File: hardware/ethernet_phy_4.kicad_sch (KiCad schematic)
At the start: 31 parts, among them J3 RJMG1S8008101BR, SW2 SW TACT-SPST, U2 DP83826IRHBR, Y2 Crystal

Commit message: Design Schematic for STM32F407
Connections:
- net RX_D4 is gone; now on net RX_D3: U2.13 (RX_D3)
- net RX_D3: no longer U2.14 (RX_D2)
- new net RX_D2: U2.14 (RX_D2)
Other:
- moved on the sheet: D6, R8
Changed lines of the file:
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@@
 	)
 	(junction
+		(at 157.48 95.25)
+		(diameter 0)
+		(color 0 0 0 0)
+	)
+	(junction
 		(at 214.63 39.37)
 		(diameter 0)
@@
 	(wire
 		(pts
-			(xy 86.36 57.15) (xy 93.98 57.15)
+			(xy 88.9 57.15) (xy 93.98 57.15)
 		)
 		(stroke
@@
 	(wire
 		(pts
-			(xy 166.37 114.3) (xy 166.37 113.03)
+			(xy 165.1 114.3) (xy 165.1 113.03)
 		)
 		(stroke
@@
 	(wire
 		(pts
+			(xy 41.91 64.77) (xy 46.99 64.77)
+		)
+		(stroke
+			(width 0)
+			(type default)
+		)
+	)
+	(wire
+		(pts
 			(xy 151.13 80.01) (xy 149.86 80.01)
 		)
@@
 	(wire
 		(pts
-			(xy 166.37 96.52) (xy 166.37 92.71)
+			(xy 165.1 96.52) (xy 165.1 92.71)
 		)
 		(stroke
@@
 	(wire
 		(pts
-			(xy 166.37 105.41) (xy 166.37 104.14)
+			(xy 165.1 105.41) (xy 165.1 104.14)
 		)
 		(stroke
@@
 	(wire
 		(pts
-			(xy 45.72 64.77) (xy 46.99 64.77)
-		)
-		(stroke
-			(width 0)
-			(type default)
-		)
-	)
-	(wire
-		(pts
 			(xy 87.63 72.39) (xy 93.98 72.39)
 		)
@@
 	(wire
 		(pts
-			(xy 166.37 92.71) (xy 149.86 92.71)
+			(xy 165.1 92.71) (xy 149.86 92.71)
 		)
 		(stroke
@@
 	(wire
 		(pts
+			(xy 158.75 95.25) (xy 157.48 95.25)
+		)
+		(stroke
+			(width 0)
+			(type default)
+		)
+	)
+	(wire
+		(pts
 			(xy 214.63 46.99) (xy 214.63 53.34)
 		)
@@
 		)
 	)
-	(label "COL"
-		(at 157.48 92.71 180)
-		(effects
-			(font
-				(size 1.27 1.27)
-			)
-			(justify right bottom)
-		)
-	)
 	(label "RD_P"
 		(at 87.63 69.85 0)
@@
 		)
 	)
-	(label "CRS"
-		(at 157.48 95.25 180)
-		(effects
-			(font
-				(size 1.27 1.27)
-			)
-			(justify right bottom)
-		)
-	)
 	(label "TD_N"
 		(at 87.63 80.01 0)
@@
 		)
 	)
+	(label "INT"
+		(at 88.9 57.15 0)
+		(effects
+			(font
+				(size 1.27 1.27)
+			)
+			(justify left bottom)
+		)
+	)
 	(label "TD_N"
 		(at 88.9 158.75 180)
@@
 		)
 	)
+	(label "INT"
+		(at 41.91 64.77 0)
+		(effects
+			(font
+				(size 1.27 1.27)
+			)
+			(justify left bottom)
+		)
+	)
 	(label "DP83826IRHBR_OSC_OUT"
 		(at 125.73 118.11 180)
@@
 		)
 	)
-	(hierarchical_label "RX_D3"
+	(hierarchical_label "CRS"
+		(shape input)
+		(at 158.75 95.25 0)
+		(effects
+			(font
+				(size 1.27 1.27)
+			)
+			(justify left)
+		)
+	)
+	(hierarchical_label "RX_D2"
 		(shape input)
 		(at 151.13 62.23 0)
@@
 		)
 	)
-	(hierarchical_label "RX_D4"
+	(hierarchical_label "RX_D3"
 		(shape input)
 		(at 151.13 64.77 0)
@@
 		)
 	)
-	(hierarchical_label "RX_D0"
+	(hierarchical_label "COL"
 		(shape input)
-		(at 151.13 57.15 0)
+		(at 165.1 92.71 0)
 		(effects
 			(font
@@
 		)
 	)
-	(hierarchical_label "TX_D3"
+	(hierarchical_label "RX_D0"
 		(shape input)
-		(at 151.13 82.55 0)
+		(at 151.13 57.15 0)
 		(effects
 			(font
@@
 		)
 	)
-	(hierarchical_label "RX_CLK"
+	(hierarchical_label "TX_D3"
 		(shape input)
-		(at 151.13 49.53 0)
+		(at 151.13 82.55 0)
 		(effects
 			(font
@@
 		)
 	)
-	(hierarchical_label "INT"
+	(hierarchical_label "RX_CLK"
 		(shape input)
-		(at 45.72 64.77 180)
+		(at 151.13 49.53 0)
 		(effects
 			(font
 				(size 1.27 1.27)
 			)
-			(justify right)
+			(justify left)
 		)
 	)
@@
 		)
 	)
-	(hierarchical_label "INT"
-		(shape input)
-		(at 86.36 57.15 180)
-		(effects
-			(font
-				(size 1.27 1.27)
-			)
-			(justify right)
-		)
-	)
 	(symbol
 		(lib_id "power:VDD")
@@
 	(symbol
 		(lib_id "STM32F407 Dev Kit Library:LED")
-		(at 166.37 109.22 90)
+		(at 165.1 109.22 90)
 		(unit 1)
 		(body_style 1)
@@
 		(dnp no)
 		(property "Reference" "D6"
-			(at 167.894 108.204 90)
+			(at 166.624 108.204 90)
 			(show_name no)
 			(do_not_autoplace no)
@@
 		)
 		(property "Value" "RED"
-			(at 167.894 110.744 90)
+			(at 166.624 110.744 90)
 			(show_name no)
 			(do_not_autoplace no)
@@
 		)
 		(property "Footprint" ""
-			(at 166.37 109.22 0)
+			(at 165.1 109.22 0)
 			(hide yes)
 			(show_name no)
@@
 		)
 		(property "Datasheet" ""
-			(at 166.37 109.22 0)
+			(at 165.1 109.22 0)
 			(hide yes)
 			(show_name no)
@@
 		)
 		(property "Description" "Light emitting diode"
-			(at 166.37 109.22 0)
+			(at 165.1 109.22 0)
 			(hide yes)
 			(show_name no)
@@
 		)
 		(property "Sim.Pins" "1=K 2=A"
-			(at 166.37 109.22 0)
+			(at 165.1 109.22 0)
 			(hide yes)
 			(show_name no)
@@
 	(symbol
 		(lib_id "power:GND")
-		(at 166.37 114.3 0)
+		(at 165.1 114.3 0)
 		(unit 1)
 		(body_style 1)
@@
 		(fields_autoplaced yes)
 		(property "Reference" "#PWR020"
-			(at 166.37 120.65 0)
+			(at 165.1 120.65 0)
 			(hide yes)
 			(show_name no)
@@
 		)
 		(property "Value" "GND"
-			(at 166.37 119.38 0)
+			(at 165.1 119.38 0)
 			(show_name no)
 			(do_not_autoplace no)
@@
 		)
 		(property "Footprint" ""
-			(at 166.37 114.3 0)
+			(at 165.1 114.3 0)
 			(hide yes)
 			(show_name no)
@@
 		)
 		(property "Datasheet" ""
-			(at 166.37 114.3 0)
+			(at 165.1 114.3 0)
 			(hide yes)
 			(show_name no)
@@
 		)
 		(property "Description" "Power symbol creates a global label with name \"GND\" , ground"
-			(at 166.37 114.3 0)
+			(at 165.1 114.3 0)
 			(hide yes)
 			(show_name no)
@@
 	(symbol
 		(lib_id "STM32F407 Dev Kit Library:R")
-		(at 166.37 100.33 0)
+		(at 165.1 100.33 0)
 		(unit 1)
 		(body_style 1)
@@
 		(dnp no)
 		(property "Reference" "R8"
-			(at 168.656 99.06 0)
+			(at 167.386 99.06 0)
 			(show_name no)
 			(do_not_autoplace no)
@@
 		)
 		(property "Value" "3k3"
-			(at 168.656 101.6 0)
+			(at 167.386 101.6 0)
 			(show_name no)
 			(do_not_autoplace no)
@@
 		)
 		(property "Footprint" ""
-			(at 164.592 100.33 90)
+			(at 163.322 100.33 90)
 			(hide yes)
 			(show_name no)
@@
 		)
 		(property "Datasheet" ""
-			(at 166.37 100.33 0)
+			(at 165.1 100.33 0)
 			(hide yes)
 			(show_name no)
@@
 		)
 		(property "Description" "Resistor"
-			(at 166.37 100.33 0)
+			(at 165.1 100.33 0)
 			(hide yes)
 			(show_name no)

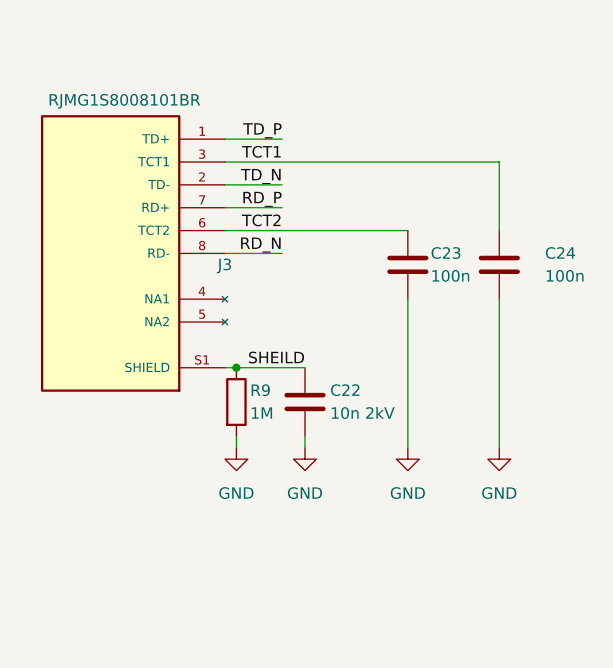
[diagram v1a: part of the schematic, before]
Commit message: Complete Schematic for Power Section
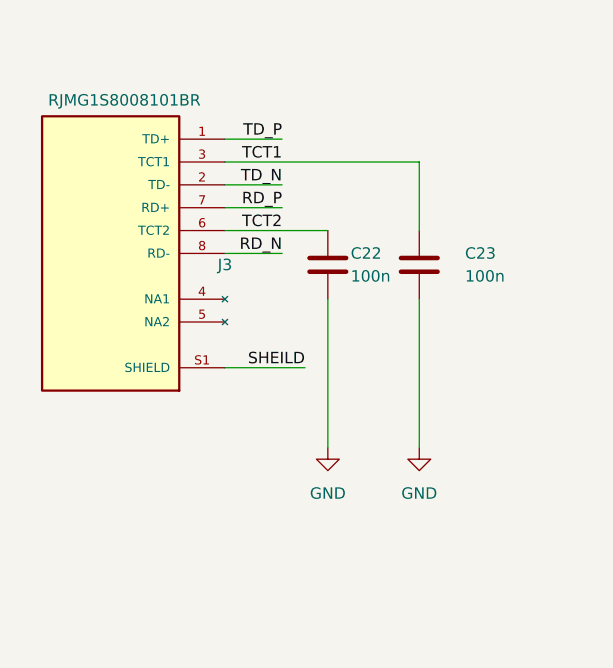
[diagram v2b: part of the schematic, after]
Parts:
- removed C22: 10n 2kV, Package_QFP:LQFP-48_7x7mm_P0.5mm, symbol STM32F407 Dev Kit Library:C
- removed R9: 1M, symbol STM32F407 Dev Kit Library:R
- renumbered C23 to C22, C24 to C23
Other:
- moved on the sheet: C22, C23

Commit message: Organize schematic
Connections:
- net GND: now also D1.2 (A), D2.2 (A), D3.2 (A), D4.2 (A)
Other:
- note added: "ESD"
- note added: "Ethernet PHY"
- note added: "Oscilator"
- note added: "RJ45 Jack"
- moved on the sheet: C11, C12, C13, C14, C15, C16, C17, C18, C19, C20, C21, C22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

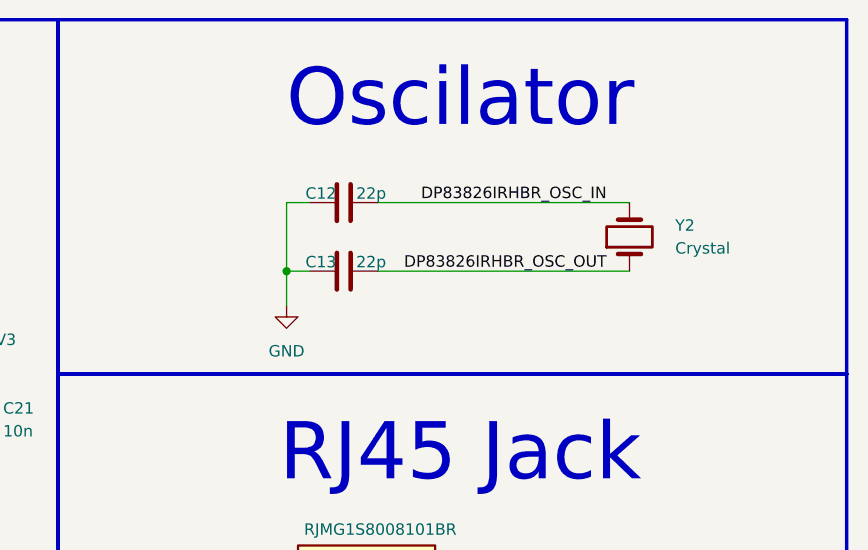
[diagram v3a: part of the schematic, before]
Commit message: Link footprints to Symbols
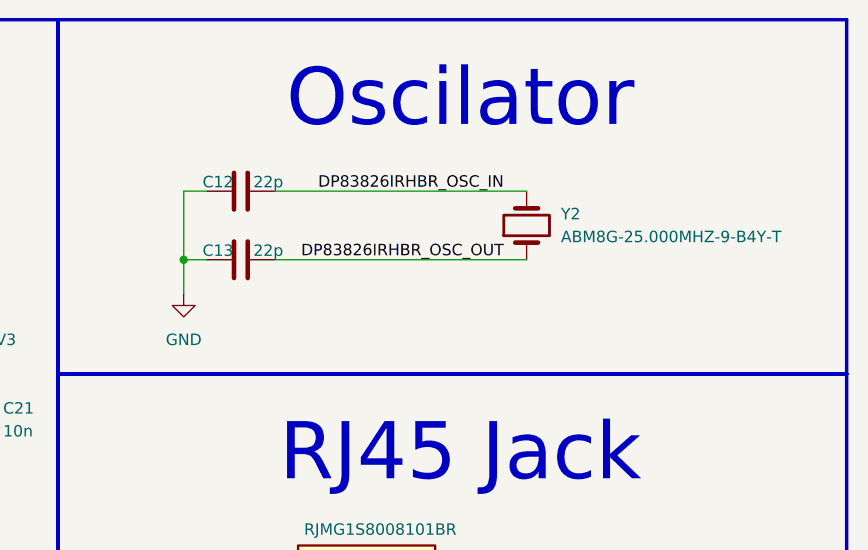
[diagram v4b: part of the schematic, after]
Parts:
- C11, C14, C15, C16, C17, C18, C19, C20, C21, C22, C23: footprint Package_QFP:LQFP-48_7x7mm_P0.5mm -> STM32F407 Dev Kit Library:C_0805_2012Metric_Pad1.18x1.45mm_HandSolder
- C12: footprint Module:ST_Morpho_Connector_144_STLink -> STM32F407 Dev Kit Library:C_0805_2012Metric_Pad1.18x1.45mm_HandSolder
- C13: footprint (none) -> STM32F407 Dev Kit Library:C_0805_2012Metric_Pad1.18x1.45mm_HandSolder
- D1, D2, D3, D4: footprint SODFL1006X43N -> STM32F407 Dev Kit Library:D_SOD-923
- D5: footprint LED_SMD:LED_Cree-XHP50_3V_HighDensity -> STM32F407 Dev Kit Library:LED_1206_3216Metric_Pad1.42x1.75mm_HandSolder
- D6: footprint (none) -> STM32F407 Dev Kit Library:LED_1206_3216Metric_Pad1.42x1.75mm_HandSolder
- FB1: footprint Package_LCC:PLCC-84_29.3x29.3mm_P1.27mm -> STM32F407 Dev Kit Library:C_0603_1608Metric_Pad1.08x0.95mm_HandSolder
- J3: footprint RJMG1S8008101BR:AMPHENOL_RJMG1S8008101BR -> STM32F407 Dev Kit Library:RJMG1S8008101BR
- R4, R6, R7: footprint DP83826IRHBR:IC_DP83826IRHBR -> STM32F407 Dev Kit Library:R_0805_2012Metric_Pad1.20x1.40mm_HandSolder
- R5, R8: footprint (none) -> STM32F407 Dev Kit Library:R_0805_2012Metric_Pad1.20x1.40mm_HandSolder
- SW2: footprint Button_Switch_SMD:Nidec_Copal_CAS-120A -> STM32F407 Dev Kit Library:SW_Push_1P1T_NO_CK_KSC9xxG
- U2: footprint DP83826IRHBR:IC_DP83826IRHBR -> STM32F407 Dev Kit Library:UQFN-32_5x5mm_P0.5mm
- Y2: value Crystal -> ABM8G-25.000MHZ-9-B4Y-T; footprint (none) -> STM32F407 Dev Kit Library:Crystal_SMD_3225-4Pin_3.2x2.5mm_HandSoldering
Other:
- moved on the sheet: C12, C13, Y2
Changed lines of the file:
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@@
 	)
 	(junction
-		(at 222.25 44.45)
+		(at 210.82 43.18)
 		(diameter 0)
 		(color 0 0 0 0)
@@
 	(wire
 		(pts
-			(xy 222.25 36.83) (xy 222.25 44.45)
+			(xy 210.82 35.56) (xy 210.82 43.18)
 		)
 		(stroke
@@
 	(wire
 		(pts
-			(xy 222.25 44.45) (xy 224.79 44.45)
+			(xy 210.82 43.18) (xy 213.36 43.18)
 		)
 		(stroke
@@
 	(wire
 		(pts
-			(xy 232.41 44.45) (xy 260.35 44.45)
+			(xy 220.98 43.18) (xy 248.92 43.18)
 		)
 		(stroke
@@
 	(wire
 		(pts
-			(xy 224.79 36.83) (xy 222.25 36.83)
+			(xy 213.36 35.56) (xy 210.82 35.56)
 		)
 		(stroke
@@
 	(wire
 		(pts
-			(xy 232.41 36.83) (xy 260.35 36.83)
+			(xy 220.98 35.56) (xy 248.92 35.56)
 		)
 		(stroke
@@
 	(wire
 		(pts
-			(xy 222.25 44.45) (xy 222.25 48.26)
+			(xy 210.82 43.18) (xy 210.82 46.99)
 		)
 		(stroke
@@
 	)
 	(label "DP83826IRHBR_OSC_OUT"
-		(at 257.81 44.45 180)
+		(at 246.38 43.18 180)
 		(effects
 			(font
@@
 	)
 	(label "DP83826IRHBR_OSC_IN"
-		(at 257.81 36.83 180)
+		(at 246.38 35.56 180)
 		(effects
 			(font
@@
 			)
 		)
-		(property "Footprint" "Package_QFP:LQFP-48_7x7mm_P0.5mm"
+		(property "Footprint" "STM32F407 Dev Kit Library:C_0805_2012Metric_Pad1.18x1.45mm_HandSolder"
 			(at 266.3952 95.25 0)
 			(hide yes)
@@
 			)
 		)
-		(property "Footprint" "Package_QFP:LQFP-48_7x7mm_P0.5mm"
+		(property "Footprint" "STM32F407 Dev Kit Library:C_0805_2012Metric_Pad1.18x1.45mm_HandSolder"
 			(at 136.8552 69.85 0)
 			(hide yes)
@@
 			)
 		)
-		(property "Footprint" "SODFL1006X43N"
+		(property "Footprint" "STM32F407 Dev Kit Library:D_SOD-923"
 			(at 134.95 149.86 0)
 			(hide yes)
@@
 	(symbol
 		(lib_id "power:GND")
-		(at 222.25 48.26 0)
+		(at 210.82 46.99 0)
 		(unit 1)
 		(body_style 1)
@@
 		(fields_autoplaced yes)
 		(property "Reference" "#PWR016"
-			(at 222.25 54.61 0)
+			(at 210.82 53.34 0)
 			(hide yes)
 			(show_name no)
@@
 		)
 		(property "Value" "GND"
-			(at 222.25 53.34 0)
+			(at 210.82 52.07 0)
 			(show_name no)
 			(do_not_autoplace no)
@@
 		)
 		(property "Footprint" ""
-			(at 222.25 48.26 0)
+			(at 210.82 46.99 0)
 			(hide yes)
 			(show_name no)
@@
 		)
 		(property "Datasheet" ""
-			(at 222.25 48.26 0)
+			(at 210.82 46.99 0)
 			(hide yes)
 			(show_name no)
@@
 		)
 		(property "Description" "Power symbol creates a global label with name \"GND\" , ground"
-			(at 222.25 48.26 0)
+			(at 210.82 46.99 0)
 			(hide yes)
 			(show_name no)
@@
 			)
 		)
-		(property "Footprint" "Package_QFP:LQFP-48_7x7mm_P0.5mm"
+		(property "Footprint" "STM32F407 Dev Kit Library:C_0805_2012Metric_Pad1.18x1.45mm_HandSolder"
 			(at 188.9252 64.77 0)
 			(hide yes)
@@
 	(symbol
 		(lib_id "STM32F407 Dev Kit Library:C")
-		(at 228.6 36.83 90)
+		(at 217.17 35.56 90)
 		(unit 1)
 		(body_style 1)
@@
 		(dnp no)
 		(property "Reference" "C12"
-			(at 226.06 35.814 90)
+			(at 214.63 34.544 90)
 			(show_name no)
 			(do_not_autoplace no)
@@
 		)
 		(property "Value" "22p"
-			(at 231.648 35.814 90)
+			(at 220.218 34.544 90)
 			(show_name no)
 			(do_not_autoplace no)
@@
 			)
 		)
-		(property "Footprint" "Module:ST_Morpho_Connector_144_STLink"
-			(at 232.41 35.8648 0)
+		(property "Footprint" "STM32F407 Dev Kit Library:C_0805_2012Metric_Pad1.18x1.45mm_HandSolder"
+			(at 220.98 34.5948 0)
 			(hide yes)
 			(show_name no)
@@
 		)
 		(property "Datasheet" ""
-			(at 228.6 36.83 0)
+			(at 217.17 35.56 0)
 			(hide yes)
 			(show_name no)
@@
 		)
 		(property "Description" "Unpolarized capacitor"
-			(at 228.6 36.83 0)
+			(at 217.17 35.56 0)
 			(hide yes)
 			(show_name no)
@@
 			)
 		)
-		(property "Footprint" "RJMG1S8008101BR:AMPHENOL_RJMG1S8008101BR"
+		(property "Footprint" "STM32F407 Dev Kit Library:RJMG1S8008101BR"
 			(at 231.14 90.17 0)
 			(hide yes)
@@
 			)
 		)
-		(property "Footprint" "Package_QFP:LQFP-48_7x7mm_P0.5mm"
+		(property "Footprint" "STM32F407 Dev Kit Library:C_0805_2012Metric_Pad1.18x1.45mm_HandSolder"
 			(at 31.4452 120.65 0)
 			(hide yes)
@@
 			)
 		)
-		(property "Footprint" ""
+		(property "Footprint" "STM32F407 Dev Kit Library:LED_1206_3216Metric_Pad1.42x1.75mm_HandSolder"
 			(at 119.38 127 0)
 			(hide yes)
@@
 	(symbol
 		(lib_id "STM32F407 Dev Kit Library:Crystal")
-		(at 260.35 40.64 90)
+		(at 248.92 39.37 90)
 		(unit 1)
 		(body_style 1)
@@
 		(fields_autoplaced yes)
 		(property "Reference" "Y2"
-			(at 265.43 39.3699 90)
+			(at 252.73 38.0999 90)
 			(show_name no)
 			(do_not_autoplace no)
@@
 			)
 		)
-		(property "Value" "Crystal"
-			(at 265.43 41.9099 90)
+		(property "Value" "ABM8G-25.000MHZ-9-B4Y-T"
+			(at 252.73 40.6399 90)
 			(show_name no)
 			(do_not_autoplace no)
@@
 			)
 		)
-		(property "Footprint" ""
-			(at 260.35 40.64 0)
+		(property "Footprint" "STM32F407 Dev Kit Library:Crystal_SMD_3225-4Pin_3.2x2.5mm_HandSoldering"
+			(at 248.92 39.37 0)
 			(hide yes)
 			(show_name no)
@@
 		)
 		(property "Datasheet" ""
-			(at 260.35 40.64 0)
+			(at 248.92 39.37 0)
 			(hide yes)
 			(show_name no)
@@
 		)
 		(property "Description" "Two pin crystal"
-			(at 260.35 40.64 0)
+			(at 248.92 39.37 0)
 			(hide yes)
 			(show_name no)
@@
 			)
 		)
-		(property "Footprint" "Package_QFP:LQFP-48_7x7mm_P0.5mm"
+		(property "Footprint" "STM32F407 Dev Kit Library:C_0805_2012Metric_Pad1.18x1.45mm_HandSolder"
 			(at 119.0752 69.85 0)
 			(hide yes)
@@
 			)
 		)
-		(property "Footprint" "Package_QFP:LQFP-48_7x7mm_P0.5mm"
+		(property "Footprint" "STM32F407 Dev Kit Library:C_0805_2012Metric_Pad1.18x1.45mm_HandSolder"
 			(at 160.9852 64.77 0)
 			(hide yes)
@@
 			)
 		)
-		(property "Footprint" "Package_QFP:LQFP-48_7x7mm_P0.5mm"
+		(property "Footprint" "STM32F407 Dev Kit Library:C_0805_2012Metric_Pad1.18x1.45mm_HandSolder"
 			(at 256.2352 95.25 0)
 			(hide yes)
@@
 			)
 		)
-		(property "Footprint" "DP83826IRHBR:IC_DP83826IRHBR"
+		(property "Footprint" "STM32F407 Dev Kit Library:UQFN-32_5x5mm_P0.5mm"
 			(at 76.2 87.63 0)
 			(hide yes)
@@
 			)
 		)
-		(property "Footprint" "SODFL1006X43N"
+		(property "Footprint" "STM32F407 Dev Kit Library:D_SOD-923"
 			(at 154 149.86 0)
 			(hide yes)
@@
 			)
 		)
-		(property "Footprint" ""
+		(property "Footprint" "STM32F407 Dev Kit Library:R_0805_2012Metric_Pad1.20x1.40mm_HandSolder"
 			(at 162.052 128.27 90)
 			(hide yes)
@@
 			)
 		)
-		(property "Footprint" "DP83826IRHBR:IC_DP83826IRHBR"
+		(property "Footprint" "STM32F407 Dev Kit Library:R_0805_2012Metric_Pad1.20x1.40mm_HandSolder"
 			(at 109.982 118.11 90)
 			(hide yes)
@@
 			)
 		)
-		(property "Footprint" "LED_SMD:LED_Cree-XHP50_3V_HighDensity"
+		(property "Footprint" "STM32F407 Dev Kit Library:LED_1206_3216Metric_Pad1.42x1.75mm_HandSolder"
 			(at 111.76 127 0)
 			(hide yes)
@@
 			)
 		)
-		(property "Footprint" "DP83826IRHBR:IC_DP83826IRHBR"
+		(property "Footprint" "STM32F407 Dev Kit Library:R_0805_2012Metric_Pad1.20x1.40mm_HandSolder"
 			(at 160.782 101.6 90)
 			(hide yes)
@@
 			)
 		)
-		(property "Footprint" "Button_Switch_SMD:Nidec_Copal_CAS-120A"
+		(property "Footprint" "STM32F407 Dev Kit Library:SW_Push_1P1T_NO_CK_KSC9xxG"
 			(at 158.75 139.7 0)
 			(hide yes)
@@
 			)
 		)
-		(property "Footprint" "Package_QFP:LQFP-48_7x7mm_P0.5mm"
+		(property "Footprint" "STM32F407 Dev Kit Library:C_0805_2012Metric_Pad1.18x1.45mm_HandSolder"
 			(at 127.9652 69.85 0)
 			(hide yes)
@@
 			)
 		)
-		(property "Footprint" "SODFL1006X43N"
+		(property "Footprint" "STM32F407 Dev Kit Library:D_SOD-923"
 			(at 115.9 149.86 0)
 			(hide yes)
@@
 			)
 		)
-		(property "Footprint" "Package_QFP:LQFP-48_7x7mm_P0.5mm"
+		(property "Footprint" "STM32F407 Dev Kit Library:C_0805_2012Metric_Pad1.18x1.45mm_HandSolder"
 			(at 178.7652 64.77 0)
 			(hide yes)
@@
 			)
 		)
-		(property "Footprint" "Package_QFP:LQFP-48_7x7mm_P0.5mm"
+		(property "Footprint" "STM32F407 Dev Kit Library:C_0805_2012Metric_Pad1.18x1.45mm_HandSolder"
 			(at 147.0152 69.85 0)
 			(hide yes)
@@
 	(symbol
 		(lib_id "STM32F407 Dev Kit Library:C")
-		(at 228.6 44.45 90)
+		(at 217.17 43.18 90)
 		(unit 1)
 		(body_style 1)
@@
 		(dnp no)
 		(property "Reference" "C13"
-			(at 226.06 43.434 90)
+			(at 214.63 42.164 90)
 			(show_name no)
 			(do_not_autoplace no)
@@
 		)
 		(property "Value" "22p"
-			(at 231.648 43.434 90)
+			(at 220.218 42.164 90)
 			(show_name no)
 			(do_not_autoplace no)
@@
 			)
 		)
-		(property "Footprint" ""
-			(at 232.41 43.4848 0)
+		(property "Footprint" "STM32F407 Dev Kit Library:C_0805_2012Metric_Pad1.18x1.45mm_HandSolder"
+			(at 220.98 42.2148 0)
 			(hide yes)
 			(show_name no)
@@
 		)
 		(property "Datasheet" ""
-			(at 228.6 44.45 0)
+			(at 217.17 43.18 0)
 			(hide yes)
 			(show_name no)
@@
 		)
 		(property "Description" "Unpolarized capacitor"
-			(at 228.6 44.45 0)
+			(at 217.17 43.18 0)
 			(hide yes)
 			(show_name no)
@@
 			)
 		)
-		(property "Footprint" "DP83826IRHBR:IC_DP83826IRHBR"
+		(property "Footprint" "STM32F407 Dev Kit Library:R_0805_2012Metric_Pad1.20x1.40mm_HandSolder"
 			(at 22.352 106.68 90)
 			(hide yes)
@@
 			)
 		)
-		(property "Footprint" "SODFL1006X43N"
+		(property "Footprint" "STM32F407 Dev Kit Library:D_SOD-923"
 			(at 173.05 149.86 0)
 			(hide yes)
@@
 			)
 		)
-		(property "Footprint" "Package_LCC:PLCC-84_29.3x29.3mm_P1.27mm"
+		(property "Footprint" "STM32F407 Dev Kit Library:C_0603_1608Metric_Pad1.08x0.95mm_HandSolder"
 			(at 154.94 58.928 90)
 			(hide yes)
@@
 			)
 		)
-		(property "Footprint" ""
+		(property "Footprint" "STM32F407 Dev Kit Library:R_0805_2012Metric_Pad1.20x1.40mm_HandSolder"
 			(at 117.602 118.11 90)
 			(hide yes)
@@
 			)
 		)
-		(property "Footprint" "Package_QFP:LQFP-48_7x7mm_P0.5mm"
+		(property "Footprint" "STM32F407 Dev Kit Library:C_0805_2012Metric_Pad1.18x1.45mm_HandSolder"
 			(at 169.8752 64.77 0)
 			(hide yes)

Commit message: Convert Schematic to PCB
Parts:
- removed Y2: ABM8G-25.000MHZ-9-B4Y-T, STM32F407 Dev Kit Library:Crystal_SMD_3225-4Pin_3.2x2.5mm_HandSoldering, symbol STM32F407 Dev Kit Library:Crystal
- added Y2: ABM8G-25.000MHZ-9-B4Y-T, STM32F407 Dev Kit Library:Crystal_SMD_3225-4Pin_3.2x2.5mm_HandSoldering, symbol Device:Crystal_GND24
- SW2: footprint STM32F407 Dev Kit Library:SW_Push_1P1T_NO_CK_KSC9xxG -> STM32F407 Dev Kit Library:SW_Push_SPST_NO_Alps_SKRK
- U2: footprint STM32F407 Dev Kit Library:UQFN-32_5x5mm_P0.5mm -> STM32F407 Dev Kit Library:DP83826IRHBR
- renumbered C14 to C12, C15 to C13, C16 to C14, C17 to C15, C18 to C16, C19 to C17, C20 to C18, C21 to C19, C12 to C20, C13 to C21, D5 to D1, D6 to D2, D1 to D3, D2 to D4, D3 to D5, D4 to D6, R6 to R4, R7 to R5, R8 to R6, R4 to R7, R5 to R8
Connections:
- net DP83826IRHBR_OSC_IN: now also Y2.1
- net DP83826IRHBR_OSC_OUT: now also Y2.3
- net GND: now also Y2.2 (G), Y2.4 (G)
- no-connect marks 0 -> 3
